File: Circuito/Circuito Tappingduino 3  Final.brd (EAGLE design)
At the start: 90.5 x 59.5 mm, 67 parts, among them IC1 LM324N

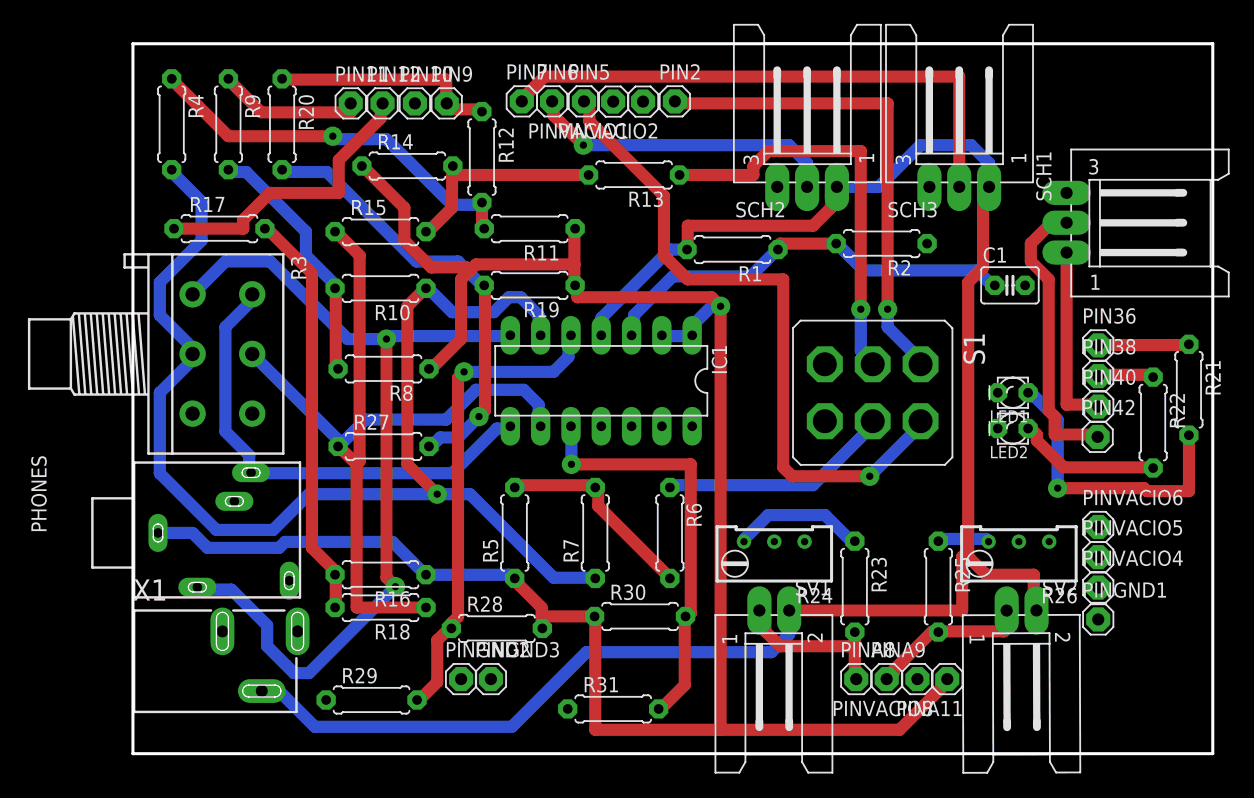
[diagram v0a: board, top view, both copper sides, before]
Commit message: COrreccion pines 11 y 12 en board
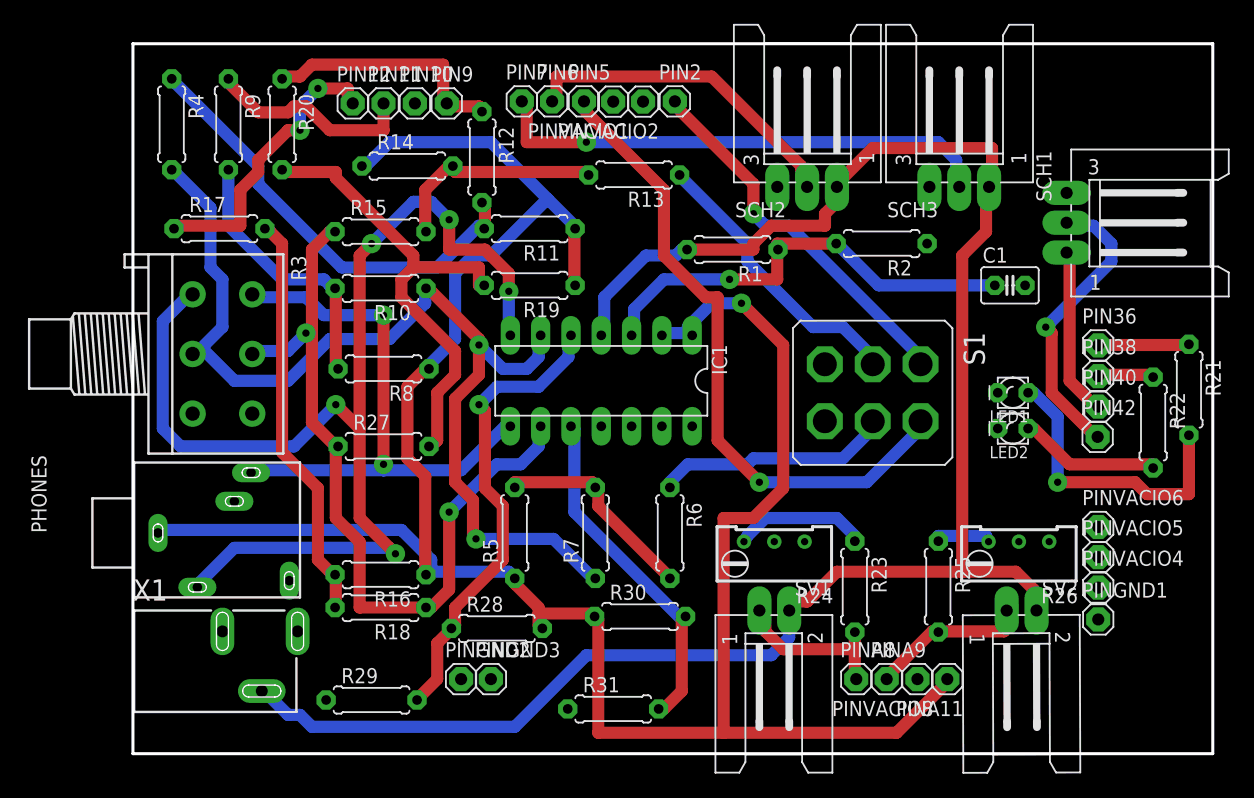
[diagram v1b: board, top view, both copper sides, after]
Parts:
- moved PIN11 2.75 mm to (34.0, 50.8)
- moved PIN12 2.50 mm to (31.4, 50.8)
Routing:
- net N$37: track 75.3 -> 100.2 mm, vias 2 -> 5
- net N$8: track 175.8 -> 198.9 mm
- net N$4: track 105.0 -> 87.2 mm, vias 1 -> 2
- net N$15: track 34.7 -> 24.0 mm, vias 1 -> 0
- net N$16: track 41.2 -> 32.3 mm
- net N$30: track 40.1 -> 48.6 mm, vias 0 -> 2
- net N$13: track 72.5 -> 66.5 mm, vias 0 -> 2
- net N$10: track 35.0 -> 29.4 mm, vias 1 -> 0
- net N$3: track 12.2 -> 17.6 mm
- net N$11: track 33.0 -> 37.4 mm, vias 1 -> 0
- net N$28: track 46.9 -> 42.6 mm, vias 0 -> 1
- net N$18: track 37.6 -> 41.1 mm, vias 1 -> 0
- net N$29: track 26.1 -> 27.9 mm, vias 1 -> 0
- net N$1: track 36.2 -> 38.1 mm, vias 0 -> 1
- net N$21: track 19.3 -> 20.8 mm
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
